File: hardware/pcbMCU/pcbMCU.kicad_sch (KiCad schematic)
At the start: 52 parts, among them J1 Conn_01x02, J2 Conn_01x04, J3 Conn_01x03, J4 Conn_01x05, SW1 SW_SPDT, U1 AMS1117-3.3, U2 AP62300, U3 STM32L412Cx, U4 Ai-Thinker-Ra-02, U5 RFM95W-915S2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

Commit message: Footprint modulo RA-02 THT creado. Pasados componentes a PCB
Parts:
- added C25: 100n, Capacitor_SMD:C_0603_1608Metric_Pad1.08x0.95mm_HandSolder, symbol Device:C_Small
- C15: footprint Capacitor_SMD:CP_Elec_6.3x5.7 -> Capacitor_THT:CP_Radial_D8.0mm_P5.00mm
- J2: footprint Connector_PinHeader_1.27mm:PinHeader_1x04_P1.27mm_Vertical -> Connector_PinHeader_2.54mm:PinHeader_1x04_P2.54mm_Vertical
- SW1: footprint Connector_PinHeader_1.27mm:PinHeader_1x03_P1.27mm_Vertical -> Connector_PinHeader_2.54mm:PinHeader_1x03_P2.54mm_Vertical
- U4: footprint RF_Module:Ai-Thinker-Ra-01-LoRa -> RF_Module:Ai-Thinker-Ra-02-LoRa-THT
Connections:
- net +3V3: now also C25.1
- net GND: now also C25.2; no longer AE1.2 (Shield)
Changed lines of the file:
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@@
     (company "Franco Montanari, Dante Conti, Maximiliano Gonzales")
   )
+  (junction (at 220.345 26.035) (diameter 0) (color 0 0 0 0)
+  )
   (junction (at 147.32 26.035) (diameter 0) (color 0 0 0 0)
   )
@@
   (junction (at 253.746 90.043) (diameter 0) (color 0 0 0 0)
   )
+  (junction (at 184.785 26.035) (diameter 0) (color 0 0 0 0)
+  )
   (junction (at 257.81 68.58) (diameter 0) (color 0 0 0 0)
   )
@@
   (junction (at 161.29 26.035) (diameter 0) (color 0 0 0 0)
   )
+  (junction (at 211.455 33.655) (diameter 0) (color 0 0 0 0)
+  )
   (junction (at 133.35 33.655) (diameter 0) (color 0 0 0 0)
   )
@@
   )
   (junction (at 198.755 33.655) (diameter 0) (color 0 0 0 0)
-  )
-  (junction (at 184.785 26.035) (diameter 0) (color 0 0 0 0)
   )
   (junction (at 155.575 154.305) (diameter 0) (color 0 0 0 0)
@@
     (stroke (width 0) (type default) (color 0 0 0 0))
   )
+  (wire (pts (xy 220.345 27.305) (xy 220.345 26.035))
+    (stroke (width 0) (type default) (color 0 0 0 0))
+  )
   (wire (pts (xy 55.245 154.94) (xy 60.325 154.94))
     (stroke (width 0) (type default) (color 0 0 0 0))
@@
     (stroke (width 0) (type default) (color 0 0 0 0))
   )
-  (wire (pts (xy 102.235 175.895) (xy 102.235 180.34))
-    (stroke (width 0) (type default) (color 0 0 0 0))
-  )
   (wire (pts (xy 211.455 26.035) (xy 211.455 27.305))
     (stroke (width 0) (type default) (color 0 0 0 0))
@@
     (stroke (width 0) (type default) (color 0 0 0 0))
   )
+  (wire (pts (xy 220.345 32.385) (xy 220.345 33.655))
+    (stroke (width 0) (type default) (color 0 0 0 0))
+  )
   (wire (pts (xy 27.305 118.745) (xy 27.305 123.825))
     (stroke (width 0) (type default) (color 0 0 0 0))
@@
     (stroke (width 0) (type default) (color 0 0 0 0))
   )
+  (wire (pts (xy 211.455 26.035) (xy 220.345 26.035))
+    (stroke (width 0) (type default) (color 0 0 0 0))
+  )
   (wire (pts (xy 184.785 32.385) (xy 184.785 33.655))
     (stroke (width 0) (type default) (color 0 0 0 0))
@@
     (stroke (width 0) (type default) (color 0 0 0 0))
   )
-  (wire (pts (xy 211.455 26.035) (xy 217.17 26.035))
-    (stroke (width 0) (type default) (color 0 0 0 0))
-  )
   (wire (pts (xy 256.54 148.59) (xy 256.54 150.495))
     (stroke (width 0) (type default) (color 0 0 0 0))
@@
     (stroke (width 0) (type default) (color 0 0 0 0))
   )
+  (wire (pts (xy 220.345 33.655) (xy 211.455 33.655))
+    (stroke (width 0) (type default) (color 0 0 0 0))
+  )
   (wire (pts (xy 92.075 173.355) (xy 92.075 174.625))
     (stroke (width 0) (type default) (color 0 0 0 0))
@@
     (stroke (width 0) (type default) (color 0 0 0 0))
   )
-  (wire (pts (xy 217.17 26.035) (xy 217.17 22.225))
+  (wire (pts (xy 220.345 26.035) (xy 220.345 22.225))
     (stroke (width 0) (type default) (color 0 0 0 0))
   )
@@
       (effects (font (size 1.27 1.27)) (justify left))
     )
-    (property "Footprint" "Capacitor_SMD:CP_Elec_6.3x5.7" (id 2) (at 39.37 33.02 0)
+    (property "Footprint" "Capacitor_THT:CP_Radial_D8.0mm_P5.00mm" (id 2) (at 39.37 33.02 0)
       (effects (font (size 1.27 1.27)) hide)
     )
@@
   (symbol (lib_id "Device:C_Small") (at 211.455 29.845 0) (unit 1)
     (in_bom yes) (on_board yes)
-    (property "Reference" "C4" (id 0) (at 215.265 28.5749 0)
-      (effects (font (size 1.27 1.27)) (justify left))
-    )
-    (property "Value" "10u" (id 1) (at 215.265 31.1149 0)
+    (property "Reference" "C4" (id 0) (at 213.995 28.575 0)
+      (effects (font (size 1.27 1.27)) (justify left))
+    )
+    (property "Value" "10u" (id 1) (at 213.995 31.115 0)
       (effects (font (size 1.27 1.27)) (justify left))
     )
@@
     )
     (property "Datasheet" "~" (id 3) (at 211.455 29.845 0)
+      (effects (font (size 1.27 1.27)) hide)
+    )
+    (pin "1")
+    (pin "2")
+  )
+  (symbol (lib_id "Device:C_Small") (at 220.345 29.845 0) (unit 1)
+    (in_bom yes) (on_board yes) (fields_autoplaced)
+    (property "Reference" "C25" (id 0) (at 223.647 28.5749 0)
+      (effects (font (size 1.27 1.27)) (justify left))
+    )
+    (property "Value" "100n" (id 1) (at 223.647 31.1149 0)
+      (effects (font (size 1.27 1.27)) (justify left))
+    )
+    (property "Footprint" "Capacitor_SMD:C_0603_1608Metric_Pad1.08x0.95mm_HandSolder" (id 2) (at 220.345 29.845 0)
+      (effects (font (size 1.27 1.27)) hide)
+    )
+    (property "Datasheet" "~" (id 3) (at 220.345 29.845 0)
       (effects (font (size 1.27 1.27)) hide)
     )
@@
     (property "Reference" "SW1" (id 0) (at 50.165 144.78 0))
     (property "Value" "SW_SPDT" (id 1) (at 50.165 147.32 0))
-    (property "Footprint" "Connector_PinHeader_1.27mm:PinHeader_1x03_P1.27mm_Vertical" (id 2) (at 50.165 152.4 0)
+    (property "Footprint" "Connector_PinHeader_2.54mm:PinHeader_1x03_P2.54mm_Vertical" (id 2) (at 50.165 152.4 0)
       (effects (font (size 1.27 1.27)) hide)
     )
@@
       (effects (font (size 1.27 1.27)) (justify left))
     )
-    (property "Footprint" "RF_Module:Ai-Thinker-Ra-01-LoRa" (id 2) (at 235.585 143.51 0)
+    (property "Footprint" "RF_Module:Ai-Thinker-Ra-02-LoRa-THT" (id 2) (at 235.585 143.51 0)
       (effects (font (size 1.27 1.27)) hide)
     )
@@
     (pin "5")
   )
-  (symbol (lib_id "power:GND") (at 102.235 180.34 0) (unit 1)
-    (in_bom yes) (on_board yes) (fields_autoplaced)
-    (property "Reference" "#PWR023" (id 0) (at 102.235 186.69 0)
-      (effects (font (size 1.27 1.27)) hide)
-    )
-    (property "Value" "GND" (id 1) (at 102.235 185.42 0))
-    (property "Footprint" "" (id 2) (at 102.235 180.34 0)
-      (effects (font (size 1.27 1.27)) hide)
-    )
-    (property "Datasheet" "" (id 3) (at 102.235 180.34 0)
-      (effects (font (size 1.27 1.27)) hide)
-    )
-    (pin "1")
-  )
   (symbol (lib_id "Mechanical:MountingHole") (at 18.415 186.055 0) (unit 1)
     (in_bom yes) (on_board yes) (fields_autoplaced)
@@
     (property "Reference" "J2" (id 0) (at 276.86 62.23 0))
     (property "Value" "Conn_01x04" (id 1) (at 276.86 64.77 0))
-    (property "Footprint" "Connector_PinHeader_1.27mm:PinHeader_1x04_P1.27mm_Vertical" (id 2) (at 276.86 73.66 0)
+    (property "Footprint" "Connector_PinHeader_2.54mm:PinHeader_1x04_P2.54mm_Vertical" (id 2) (at 276.86 73.66 0)
       (effects (font (size 1.27 1.27)) hide)
     )
@@
     (pin "2")
   )
-  (symbol (lib_id "power:+3V3") (at 217.17 22.225 0) (unit 1)
-    (in_bom yes) (on_board yes) (fields_autoplaced)
-    (property "Reference" "#PWR07" (id 0) (at 217.17 26.035 0)
-      (effects (font (size 1.27 1.27)) hide)
-    )
-    (property "Value" "+3V3" (id 1) (at 217.17 17.145 0))
-    (property "Footprint" "" (id 2) (at 217.17 22.225 0)
-      (effects (font (size 1.27 1.27)) hide)
-    )
-    (property "Datasheet" "" (id 3) (at 217.17 22.225 0)
+  (symbol (lib_id "power:+3V3") (at 220.345 22.225 0) (unit 1)
+    (in_bom yes) (on_board yes) (fields_autoplaced)
+    (property "Reference" "#PWR07" (id 0) (at 220.345 26.035 0)
+      (effects (font (size 1.27 1.27)) hide)
+    )
+    (property "Value" "+3V3" (id 1) (at 220.345 17.145 0))
+    (property "Footprint" "" (id 2) (at 220.345 22.225 0)
+      (effects (font (size 1.27 1.27)) hide)
+    )
+    (property "Datasheet" "" (id 3) (at 220.345 22.225 0)
       (effects (font (size 1.27 1.27)) hide)
     )
@@
       (reference "#PWR022") (unit 1) (value "GND") (footprint "")
     )
-    (path "/8abb8d1a-6379-4256-8d99-3a0b76d4b627"
-      (reference "#PWR023") (unit 1) (value "GND") (footprint "")
-    )
     (path "/1be9a059-4a10-4a93-9b2f-0f98707dcac2"
       (reference "#PWR024") (unit 1) (value "GND") (footprint "")
@@
     )
     (path "/150339cd-3d42-426a-bc1e-f1f725ca6a46"
-      (reference "C15") (unit 1) (value "100u") (footprint "Capacitor_SMD:CP_Elec_6.3x5.7")
+      (reference "C15") (unit 1) (value "100u") (footprint "Capacitor_THT:CP_Radial_D8.0mm_P5.00mm")
     )
     (path "/dc535bd2-0afa-43cc-b360-fcdeae8e91d1"
@@
       (reference "C24") (unit 1) (value "1u") (footprint "Capacitor_SMD:C_0805_2012Metric_Pad1.18x1.45mm_HandSolder")
     )
+    (path "/4cef2415-29b9-4ac7-b4fa-b9369a01fede"
+      (reference "C25") (unit 1) (value "100n") (footprint "Capacitor_SMD:C_0603_1608Metric_Pad1.08x0.95mm_HandSolder")
+    )
     (path "/d00cff67-6cb0-47ac-a376-f0ea8ed8cead"
       (reference "D1") (unit 1) (value "D_Schottky_Small") (footprint "Diode_SMD:D_0201_0603Metric_Pad0.64x0.40mm_HandSolder")
@@
     )
     (path "/acb54d58-a2e6-410e-a731-a5c04e5d4663"
-      (reference "J2") (unit 1) (value "Conn_01x04") (footprint "Connector_PinHeader_1.27mm:PinHeader_1x04_P1.27mm_Vertical")
+      (reference "J2") (unit 1) (value "Conn_01x04") (footprint "Connector_PinHeader_2.54mm:PinHeader_1x04_P2.54mm_Vertical")
     )
     (path "/07144b2b-e321-4056-8c50-89e995b0a11d"
@@
     )
     (path "/7729dfdb-a7ad-44cc-85af-d34fc833756a"
-      (reference "SW1") (unit 1) (value "SW_SPDT") (footprint "Connector_PinHeader_1.27mm:PinHeader_1x03_P1.27mm_Vertical")
+      (reference "SW1") (unit 1) (value "SW_SPDT") (footprint "Connector_PinHeader_2.54mm:PinHeader_1x03_P2.54mm_Vertical")
     )
     (path "/779b8552-86f5-4730-b34c-5cb68bd99eed"
@@
     )
     (path "/820c19e2-bf85-4bb2-a568-8451156493f9"
-      (reference "U4") (unit 1) (value "Ai-Thinker-Ra-02") (footprint "RF_Module:Ai-Thinker-Ra-01-LoRa")
+      (reference "U4") (unit 1) (value "Ai-Thinker-Ra-02") (footprint "RF_Module:Ai-Thinker-Ra-02-LoRa-THT")
     )
     (path "/1c517d28-8355-4dad-a63e-2ee60e86f689"

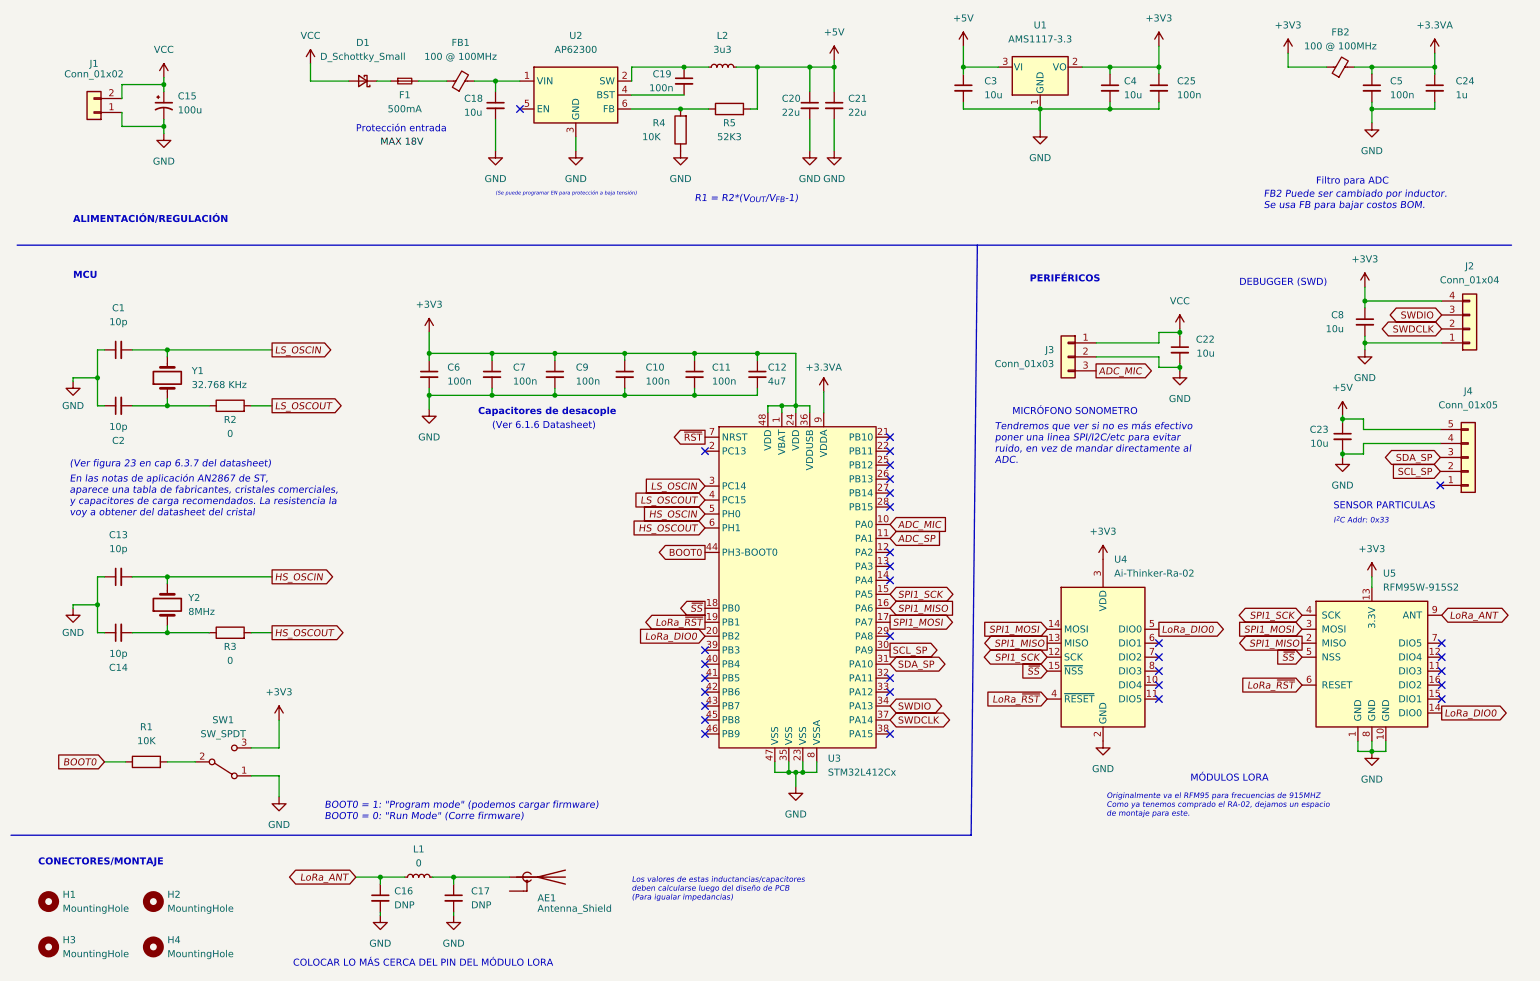
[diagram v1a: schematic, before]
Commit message: Cambio a ESP32
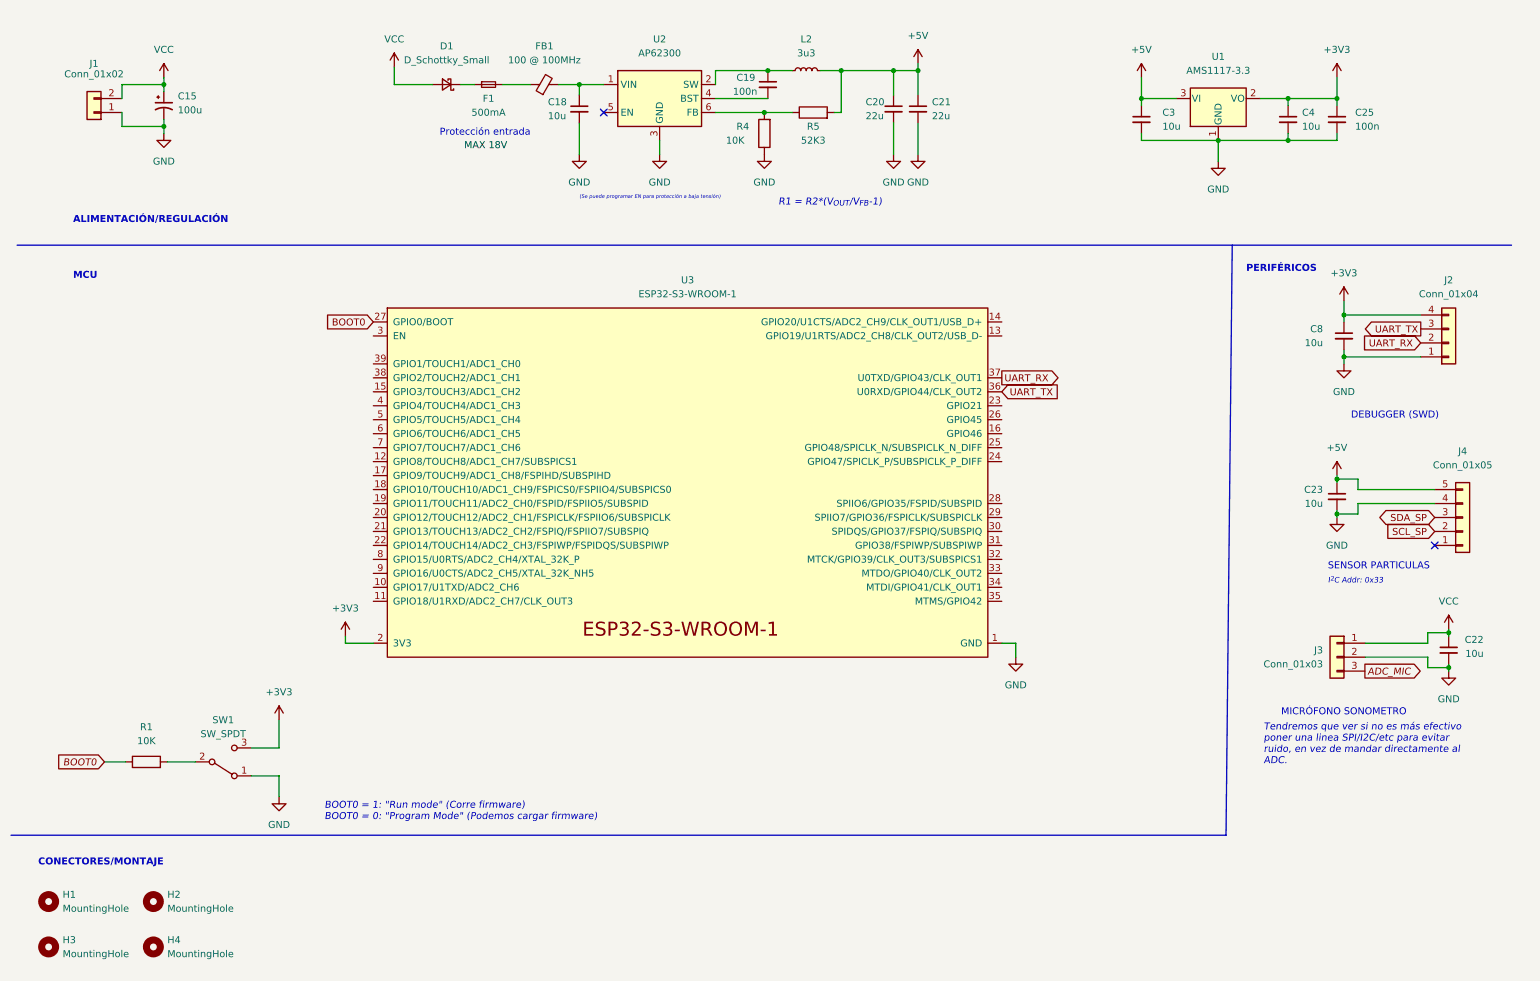
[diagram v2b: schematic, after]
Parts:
- removed AE1: Antenna_Shield, Connector_Coaxial:SMA_Amphenol_132203-12_Horizontal, symbol Device:Antenna_Shield
- removed C1, C13, C14, C2: 10p, Capacitor_SMD:C_0603_1608Metric_Pad1.08x0.95mm_HandSolder, symbol Device:C_Small
- removed C10, C11, C5, C6, C7, C9: 100n, Capacitor_SMD:C_0603_1608Metric_Pad1.08x0.95mm_HandSolder, symbol Device:C_Small
- removed C12: 4u7, Capacitor_SMD:C_0805_2012Metric_Pad1.18x1.45mm_HandSolder, symbol Device:C_Small
- removed C16, C17: DNP, Capacitor_SMD:C_0603_1608Metric_Pad1.08x0.95mm_HandSolder, symbol Device:C_Small
- removed C24: 1u, Capacitor_SMD:C_0805_2012Metric_Pad1.18x1.45mm_HandSolder, symbol Device:C_Small
- removed FB2: 100 @ 100MHz, Inductor_SMD:L_0603_1608Metric_Pad1.05x0.95mm_HandSolder, symbol Device:FerriteBead_Small
- removed L1: 0, Inductor_SMD:L_0603_1608Metric_Pad1.05x0.95mm_HandSolder, symbol Device:L_Small
- removed R2, R3: 0, Resistor_SMD:R_0603_1608Metric_Pad0.98x0.95mm_HandSolder, symbol Device:R
- removed U3: STM32L412Cx, Package_QFP:LQFP-48-1EP_7x7mm_P0.5mm_EP3.6x3.6mm_ThermalVias, symbol MCU_ST_STM32L4:STM32L412Cx
- removed U4: Ai-Thinker-Ra-02, RF_Module:Ai-Thinker-Ra-02-LoRa-THT, symbol RF_Module:Ai-Thinker-Ra-02
- removed U5: RFM95W-915S2, pcbMCU:XCVR_RFM95W-915S2, symbol RF_Module:RFM95W-915S2
- removed Y1: 32.768 KHz, Crystal:Crystal_SMD_0603-2Pin_6.0x3.5mm_HandSoldering, symbol Device:Crystal
- removed Y2: 8MHz, Crystal:Crystal_SMD_0603-2Pin_6.0x3.5mm_HandSoldering, symbol Device:Crystal
- added U3: ESP32-S3-WROOM-1, RF_Module:ESP32-S3-WROOM-1U, symbol Espressif:ESP32-S3-WROOM-1
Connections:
- net +3V3: now also U3.2 (3V3)
- net BOOT0: now also U3.27 (GPIO0/BOOT)
- net GND: now also U3.1 (GND), U3.40 (GND), U3.41 (GND)
- net SWDCLK renamed UART_RX
- net UART_RX: now also U3.37 (U0TXD/GPIO43/CLK_OUT1)
- net SWDIO renamed UART_TX
- net UART_TX: now also U3.36 (U0RXD/GPIO44/CLK_OUT2)
- no-connect marks 33 -> 2
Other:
- note added: "BOOT0 = 1: "Run mode" (Corre firmware) BOOT0 = 0: "Program Mode" (Podemos cargar firmware)"
- note removed: "(Ver 6.1.6 Datasheet)"
- note removed: "(Ver figura 23 en cap 6.3.7 del datasheet)"
- note removed: "BOOT0 = 1: "Program mode" (podemos cargar firmware) BOOT0 = 0: "Run Mode" (Corre firmware)"
- note removed: "COLOCAR LO MÁS CERCA DEL PIN DEL MÓDULO LORA"
- note removed: "Capacitores de desacople"
- note removed: "En las notas de aplicación AN2867 de ST, aparece una tabla de fabricantes, cristales comerciales, y capacitores de carga recomendados. La resistencia la voy a obtener del datasheet del cristal"
- note removed: "FB2 Puede ser cambiado por inductor. Se usa FB para bajar costos BOM."
- note removed: "Filtro para ADC"
- note removed: "Los valores de estas inductancias/capacitores deben calcularse luego del diseño de PCB (Para igualar impedancias)"
- note removed: "MÓDULOS LORA"
- note removed: "Originalmente va el RFM95 para frecuencias de 915MHZ Como ya tenemos comprado el RA-02, dejamos un espacio de montaje para este."
- moved on the sheet: C18, C19, C20, C21, C22, C23, C25, C3, C4, C8, D1, F1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
